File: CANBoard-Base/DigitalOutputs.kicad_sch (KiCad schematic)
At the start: 4 parts

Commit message: Switched to v2
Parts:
- F1: footprint (none) -> Fuse:Fuse_0805_2012Metric
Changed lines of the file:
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@@
       (effects (font (size 1.27 1.27)))
     )
-    (property "Footprint" "" (at 134.62 74.93 0)
+    (property "Footprint" "Fuse:Fuse_0805_2012Metric" (at 134.62 74.93 0)
       (effects (font (size 1.27 1.27)) (justify left) hide)
     )
@@
       (effects (font (size 1.27 1.27)))
     )
-    (property "Footprint" "" (at 134.62 87.63 0)
+    (property "Footprint" "Fuse:Fuse_0805_2012Metric" (at 134.62 87.63 0)
       (effects (font (size 1.27 1.27)) (justify left) hide)
     )
@@
       (effects (font (size 1.27 1.27)))
     )
-    (property "Footprint" "" (at 134.62 62.23 0)
+    (property "Footprint" "Fuse:Fuse_0805_2012Metric" (at 134.62 62.23 0)
       (effects (font (size 1.27 1.27)) (justify left) hide)
     )
@@
       (effects (font (size 1.27 1.27)))
     )
-    (property "Footprint" "" (at 134.62 49.53 0)
+    (property "Footprint" "Fuse:Fuse_0805_2012Metric" (at 134.62 49.53 0)
       (effects (font (size 1.27 1.27)) (justify left) hide)
     )

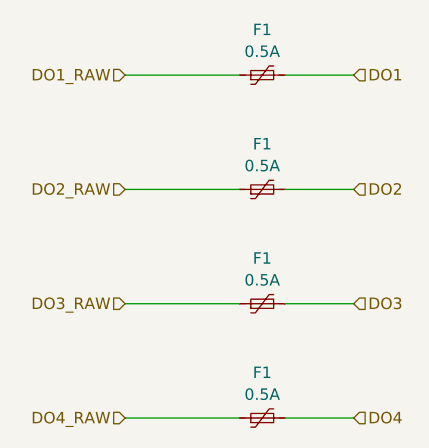
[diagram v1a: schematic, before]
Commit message: Update to Kicad 8
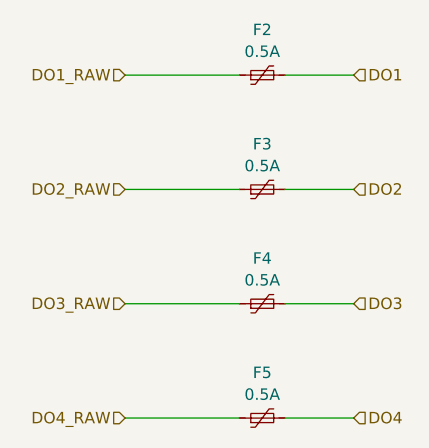
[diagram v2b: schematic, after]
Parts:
- renumbered F1 to F2, F1 to F3, F1 to F4, F1 to F5

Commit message: as built v1
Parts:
- F2, F3, F4, F5: JLC_PN (none) -> C22378359
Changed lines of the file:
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@@
+			)
+		)
+		(property "JLC_PN" "C22378359"
+			(at 129.54 76.2 0)
+			(effects
+				(font
+					(size 1.27 1.27)
+				)
+				(hide yes)
 			)
 		)
@@
 			)
 		)
+		(property "JLC_PN" "C22378359"
+			(at 129.54 88.9 0)
+			(effects
+				(font
+					(size 1.27 1.27)
+				)
+				(hide yes)
+			)
+		)
 		(pin "1"
 		)
@@
 			)
 		)
+		(property "JLC_PN" "C22378359"
+			(at 129.54 63.5 0)
+			(effects
+				(font
+					(size 1.27 1.27)
+				)
+				(hide yes)
+			)
+		)
 		(pin "1"
 		)
@@
 			(at 129.54 50.8 0)
 			(effects
+				(font
+					(size 1.27 1.27)
+				)
+				(hide yes)
+			)
+		)
+		(property "JLC_PN" "C22378359"
+			(at 129.54 50.8 0)
+			(effects
